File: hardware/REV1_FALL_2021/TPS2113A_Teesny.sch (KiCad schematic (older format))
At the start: 6 parts, among them U201 TPS2113ADRBR

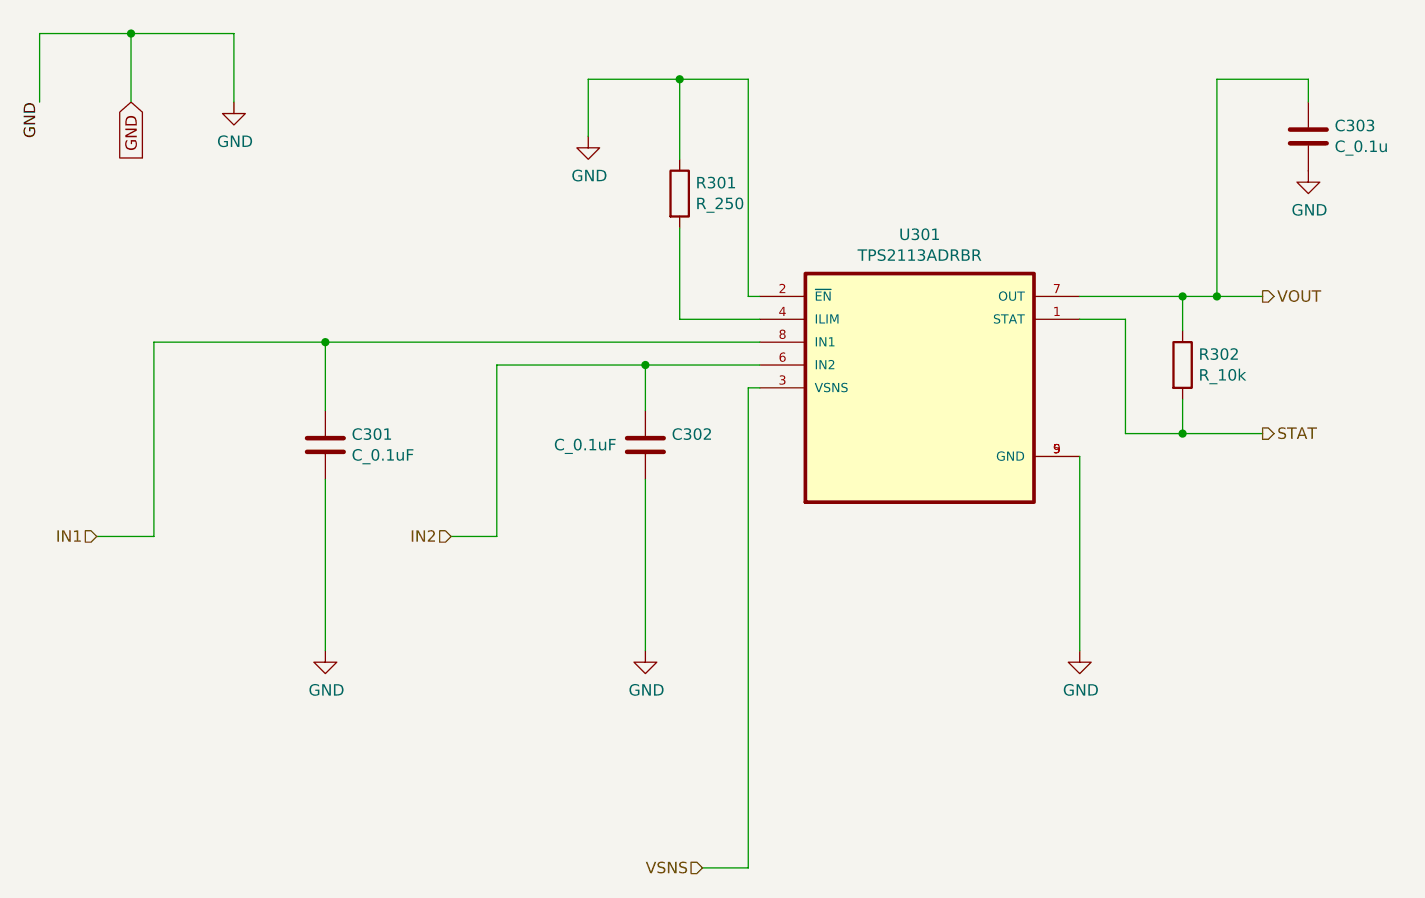
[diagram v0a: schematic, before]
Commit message: Change footprint of TPS2113A to the TSSOP package
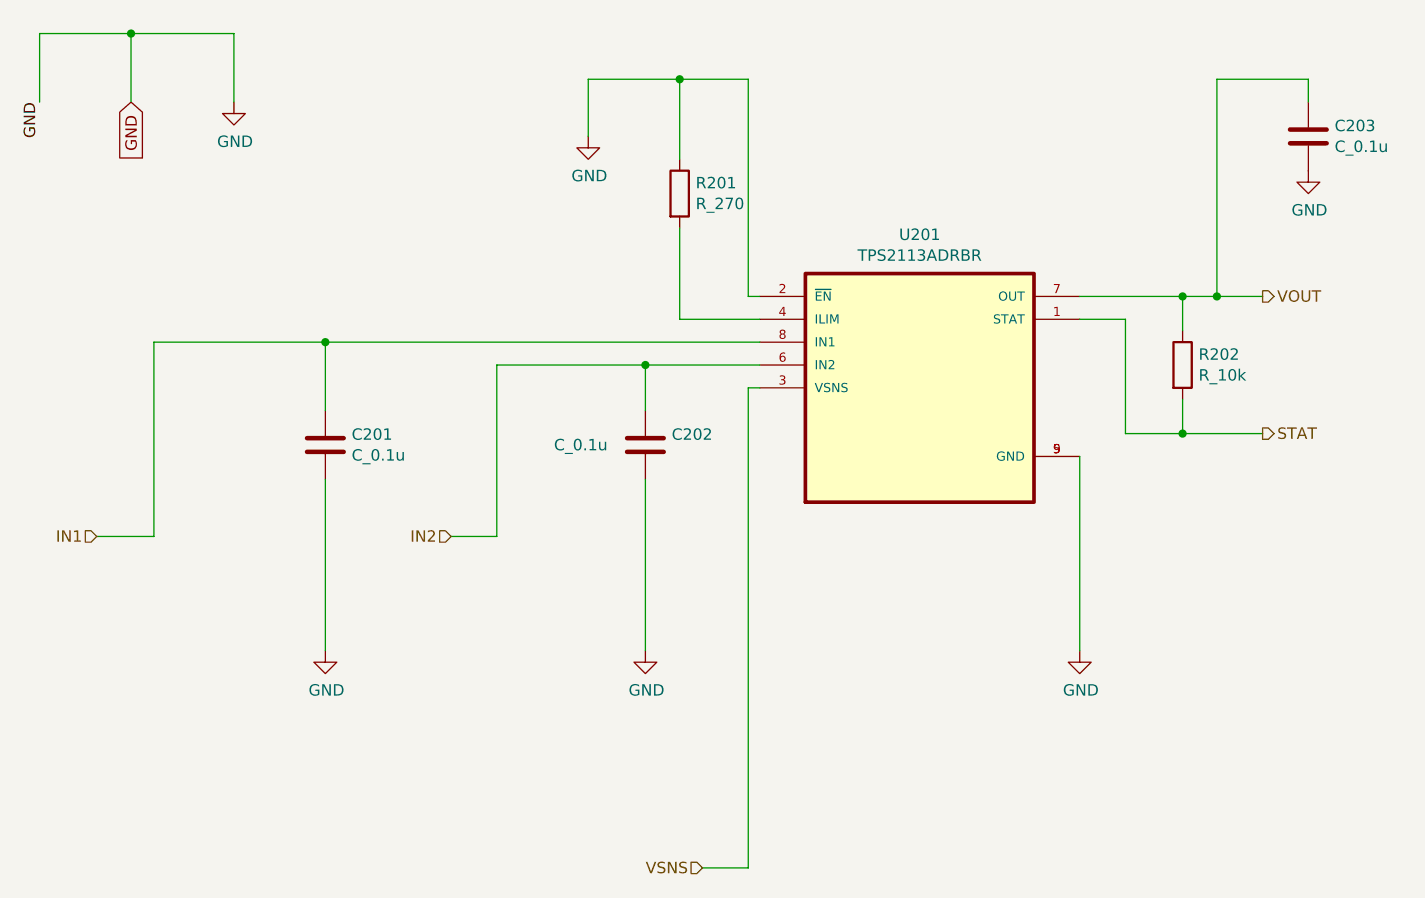
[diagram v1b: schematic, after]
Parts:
- C301, C302: value C_0.1uF -> C_0.1u
- R301: value R_250 -> R_270
- U201: footprint footprints:TPS2113ADRBR -> Package_SO:TSSOP-8_4.4x3mm_P0.65mm
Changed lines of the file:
@@
 AR Path="/61A02CEE/61AB462E" Ref="U201"  Part="1"
 AR Path="/619AC3BC/61AB462E" Ref="U301"  Part="1"
-F 0 "U301" H 6600 3720 50  0000 C CNN
+F 0 "U201" H 6600 3720 50  0000 C CNN
 F 1 "TPS2113ADRBR" H 6600 3629 50  0000 C CNN
-F 2 "footprints:TPS2113ADRBR" H 6600 3050 50  0001 L BNN
+F 2 "Package_SO:TSSOP-8_4.4x3mm_P0.65mm" H 6600 3050 50  0001 L BNN
 F 3 "https://www.ti.com/lit/ds/symlink/tps2113a.pdf" H 6600 3050 50  0001 L BNN
 	1    6600 3050
@@
 AR Path="/619AC3BC/61AB4644" Ref="C301"  Part="1"
 AR Path="/61A02CEE/61AB4644" Ref="C201"  Part="1"
-F 0 "C301" H 4115 3346 50  0000 L CNN
-F 1 "C_0.1uF" H 4115 3255 50  0000 L CNN
+F 0 "C201" H 4115 3346 50  0000 L CNN
+F 1 "C_0.1u" H 4115 3255 50  0000 L CNN
 F 2 "Capacitor_SMD:C_0805_2012Metric_Pad1.18x1.45mm_HandSolder" H 4038 3150 50  0001 C CNN
 F 3 "~" H 4000 3300 50  0001 C CNN
@@
 AR Path="/619AC3BC/61AB464C" Ref="C302"  Part="1"
 AR Path="/61A02CEE/61AB464C" Ref="C202"  Part="1"
-F 0 "C302" H 5515 3346 50  0000 L CNN
-F 1 "C_0.1uF" H 5000 3300 50  0000 L CNN
+F 0 "C202" H 5515 3346 50  0000 L CNN
+F 1 "C_0.1u" H 5000 3300 50  0000 L CNN
 F 2 "Capacitor_SMD:C_0805_2012Metric_Pad1.18x1.45mm_HandSolder" H 5438 3150 50  0001 C CNN
 F 3 "~" H 5400 3300 50  0001 C CNN
@@
 AR Path="/619AC3BC/61AB465E" Ref="R301"  Part="1"
 AR Path="/61A02CEE/61AB465E" Ref="R201"  Part="1"
-F 0 "R301" H 5620 2246 50  0000 L CNN
-F 1 "R_250" H 5620 2155 50  0000 L CNN
+F 0 "R201" H 5620 2246 50  0000 L CNN
+F 1 "R_270" H 5620 2155 50  0000 L CNN
 F 2 "Resistor_SMD:R_0805_2012Metric_Pad1.20x1.40mm_HandSolder" V 5480 2200 50  0001 C CNN
 F 3 "~" H 5550 2200 50  0001 C CNN
@@
 AR Path="/619AC3BC/61AB4669" Ref="#PWR0113"  Part="1"
 AR Path="/61A02CEE/61AB4669" Ref="#PWR0121"  Part="1"
-F 0 "#PWR0113" H 5150 1700 50  0001 C CNN
+F 0 "#PWR0121" H 5150 1700 50  0001 C CNN
 F 1 "GND" H 5155 1777 50  0000 C CNN
 F 2 "" H 5150 1950 50  0001 C CNN
@@
 AR Path="/619AC3BC/61AB4675" Ref="#PWR0115"  Part="1"
 AR Path="/61A02CEE/61AB4675" Ref="#PWR0123"  Part="1"
-F 0 "#PWR0115" H 4000 3950 50  0001 C CNN
+F 0 "#PWR0123" H 4000 3950 50  0001 C CNN
 F 1 "GND" H 4005 4027 50  0000 C CNN
 F 2 "" H 4000 4200 50  0001 C CNN
@@
 AR Path="/619AC3BC/61AB4681" Ref="#PWR0117"  Part="1"
 AR Path="/61A02CEE/61AB4681" Ref="#PWR0125"  Part="1"
-F 0 "#PWR0117" H 5400 3950 50  0001 C CNN
+F 0 "#PWR0125" H 5400 3950 50  0001 C CNN
 F 1 "GND" H 5405 4027 50  0000 C CNN
 F 2 "" H 5400 4200 50  0001 C CNN
@@
 AR Path="/619AC3BC/61AB4687" Ref="#PWR0118"  Part="1"
 AR Path="/61A02CEE/61AB4687" Ref="#PWR0126"  Part="1"
-F 0 "#PWR0118" H 7300 3950 50  0001 C CNN
+F 0 "#PWR0126" H 7300 3950 50  0001 C CNN
 F 1 "GND" H 7305 4027 50  0000 C CNN
 F 2 "" H 7300 4200 50  0001 C CNN
@@
 AR Path="/619AC3BC/61AB46B4" Ref="R302"  Part="1"
 AR Path="/61A02CEE/61AB46B4" Ref="R202"  Part="1"
-F 0 "R302" H 7820 2996 50  0000 L CNN
+F 0 "R202" H 7820 2996 50  0000 L CNN
 F 1 "R_10k" H 7820 2905 50  0000 L CNN
 F 2 "Resistor_SMD:R_0805_2012Metric_Pad1.20x1.40mm_HandSolder" V 7680 2950 50  0001 C CNN
@@
 AR Path="/619AC3BC/61AB46C3" Ref="C303"  Part="1"
 AR Path="/61A02CEE/61AB46C3" Ref="C203"  Part="1"
-F 0 "C303" H 8415 1996 50  0000 L CNN
+F 0 "C203" H 8415 1996 50  0000 L CNN
 F 1 "C_0.1u" H 8415 1905 50  0000 L CNN
 F 2 "Capacitor_SMD:C_0805_2012Metric_Pad1.18x1.45mm_HandSolder" H 8338 1800 50  0001 C CNN
@@
 AR Path="/619AC3BC/61AB46CF" Ref="#PWR0119"  Part="1"
 AR Path="/61A02CEE/61AB46CF" Ref="#PWR0127"  Part="1"
-F 0 "#PWR0119" H 8300 1850 50  0001 C CNN
+F 0 "#PWR0127" H 8300 1850 50  0001 C CNN
 F 1 "GND" H 8305 1927 50  0000 C CNN
 F 2 "" H 8300 2100 50  0001 C CNN
@@
 AR Path="/619AC3BC/61ABB0D4" Ref="#PWR0120"  Part="1"
 AR Path="/61A02CEE/61ABB0D4" Ref="#PWR0128"  Part="1"
-F 0 "#PWR0120" H 3600 1550 50  0001 C CNN
+F 0 "#PWR0128" H 3600 1550 50  0001 C CNN
 F 1 "GND" H 3605 1627 50  0000 C CNN
 F 2 "" H 3600 1800 50  0001 C CNN

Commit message: add series resistor to improve accuracy of ILIM resistor
It used to be a 400 ohm resistor, but those are not in stock in JLC's assembly parts. Now it is two 200 ohm resistors in series. It is important to get the values precise, because the maximum rating of the (inferior, but the only one in stock) TPS2113A is 1.25A, which is also the minimum all-fire current on the E-matches. So we need exactly 1.25A, not above, and not below.
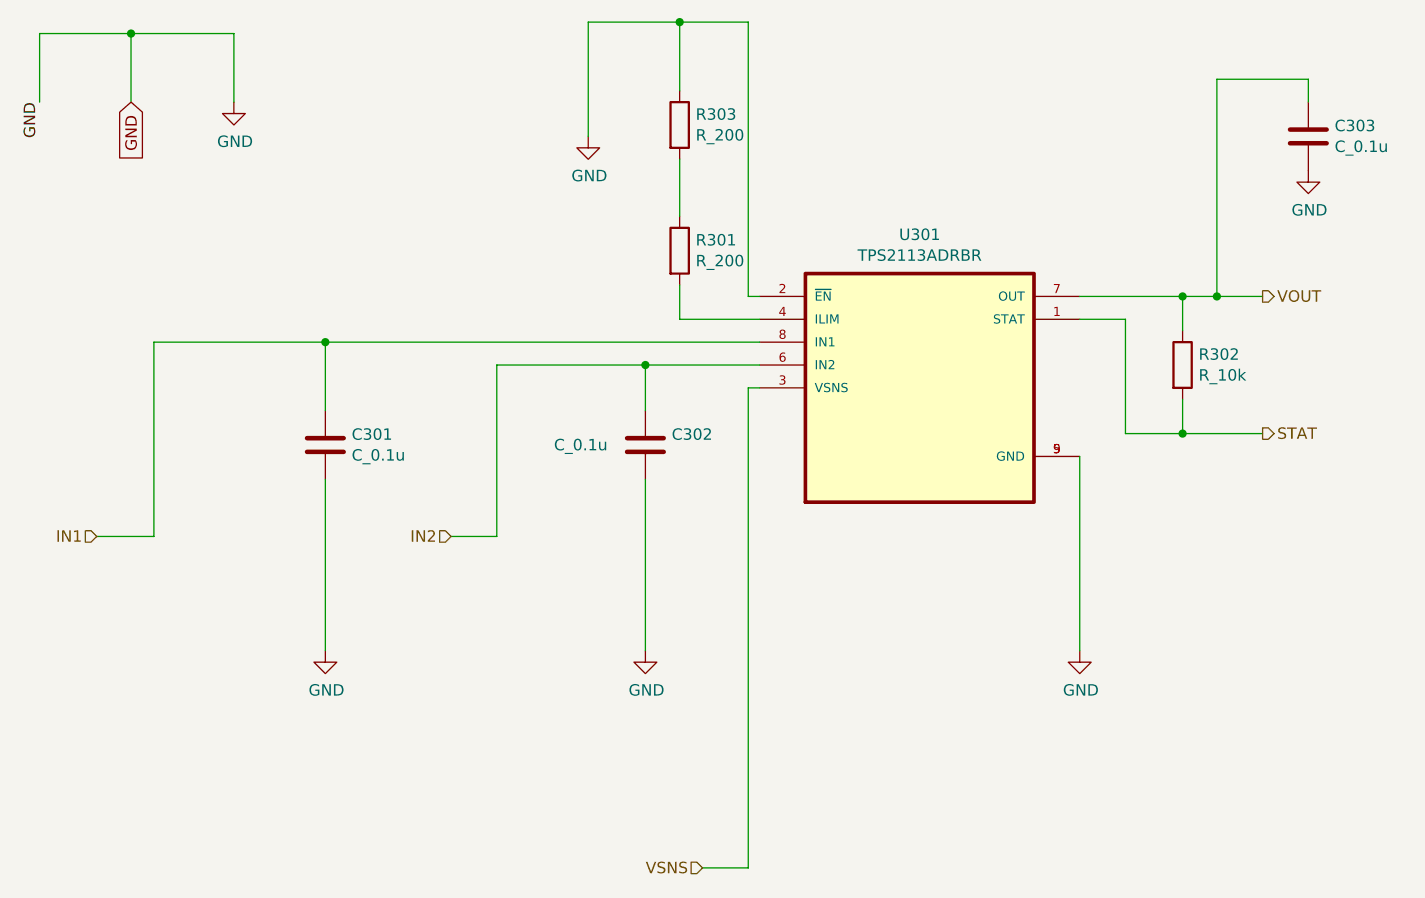
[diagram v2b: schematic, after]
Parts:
- added R303: R_200, Resistor_SMD:R_0805_2012Metric_Pad1.20x1.40mm_HandSolder, symbol Device:R
- R301: value R_270 -> R_200
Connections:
- net GND: now also R303.1; no longer R301.1
- new net: R301.1, R303.2
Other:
- moved on the sheet: R301
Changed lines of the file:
@@
 AR Path="/61A02CEE/61AB462E" Ref="U201"  Part="1"
 AR Path="/619AC3BC/61AB462E" Ref="U301"  Part="1"
-F 0 "U201" H 6600 3720 50  0000 C CNN
+F 0 "U301" H 6600 3720 50  0000 C CNN
 F 1 "TPS2113ADRBR" H 6600 3629 50  0000 C CNN
 F 2 "Package_SO:TSSOP-8_4.4x3mm_P0.65mm" H 6600 3050 50  0001 L BNN
@@
 AR Path="/619AC3BC/61AB4644" Ref="C301"  Part="1"
 AR Path="/61A02CEE/61AB4644" Ref="C201"  Part="1"
-F 0 "C201" H 4115 3346 50  0000 L CNN
+F 0 "C301" H 4115 3346 50  0000 L CNN
 F 1 "C_0.1u" H 4115 3255 50  0000 L CNN
 F 2 "Capacitor_SMD:C_0805_2012Metric_Pad1.18x1.45mm_HandSolder" H 4038 3150 50  0001 C CNN
@@
 AR Path="/619AC3BC/61AB464C" Ref="C302"  Part="1"
 AR Path="/61A02CEE/61AB464C" Ref="C202"  Part="1"
-F 0 "C202" H 5515 3346 50  0000 L CNN
+F 0 "C302" H 5515 3346 50  0000 L CNN
 F 1 "C_0.1u" H 5000 3300 50  0000 L CNN
 F 2 "Capacitor_SMD:C_0805_2012Metric_Pad1.18x1.45mm_HandSolder" H 5438 3150 50  0001 C CNN
@@
 	5900 2650 5850 2650
 Wire Wire Line
-	5850 2650 5850 1700
-Wire Wire Line
 	5900 2750 5550 2750
 Wire Wire Line
-	5550 2750 5550 2350
+	5550 2750 5550 2600
 $Comp
 L Device:R R?
 U 1 1 61AB465E
-P 5550 2200
+P 5550 2450
 AR Path="/61AB465E" Ref="R?"  Part="1"
 AR Path="/619AC3BC/61AB465E" Ref="R301"  Part="1"
 AR Path="/61A02CEE/61AB465E" Ref="R201"  Part="1"
-F 0 "R201" H 5620 2246 50  0000 L CNN
-F 1 "R_270" H 5620 2155 50  0000 L CNN
-F 2 "Resistor_SMD:R_0805_2012Metric_Pad1.20x1.40mm_HandSolder" V 5480 2200 50  0001 C CNN
-F 3 "~" H 5550 2200 50  0001 C CNN
-	1    5550 2200
-	1    0    0    -1
-$EndComp
-Wire Wire Line
-	5550 2050 5550 1700
-Wire Wire Line
-	5550 1700 5850 1700
-Wire Wire Line
-	5550 1700 5150 1700
-Wire Wire Line
-	5150 1700 5150 1950
-Connection ~ 5550 1700
+F 0 "R301" H 5620 2496 50  0000 L CNN
+F 1 "R_200" H 5620 2405 50  0000 L CNN
+F 2 "Resistor_SMD:R_0805_2012Metric_Pad1.20x1.40mm_HandSolder" V 5480 2450 50  0001 C CNN
+F 3 "~" H 5550 2450 50  0001 C CNN
+	1    5550 2450
+	1    0    0    -1
+$EndComp
+Wire Wire Line
+	5550 2300 5550 2050
 $Comp
 L power:GND #PWR?
@@
 AR Path="/619AC3BC/61AB4669" Ref="#PWR0113"  Part="1"
 AR Path="/61A02CEE/61AB4669" Ref="#PWR0121"  Part="1"
-F 0 "#PWR0121" H 5150 1700 50  0001 C CNN
+F 0 "#PWR0113" H 5150 1700 50  0001 C CNN
 F 1 "GND" H 5155 1777 50  0000 C CNN
 F 2 "" H 5150 1950 50  0001 C CNN
@@
 AR Path="/619AC3BC/61AB4675" Ref="#PWR0115"  Part="1"
 AR Path="/61A02CEE/61AB4675" Ref="#PWR0123"  Part="1"
-F 0 "#PWR0123" H 4000 3950 50  0001 C CNN
+F 0 "#PWR0115" H 4000 3950 50  0001 C CNN
 F 1 "GND" H 4005 4027 50  0000 C CNN
 F 2 "" H 4000 4200 50  0001 C CNN
@@
 AR Path="/619AC3BC/61AB4681" Ref="#PWR0117"  Part="1"
 AR Path="/61A02CEE/61AB4681" Ref="#PWR0125"  Part="1"
-F 0 "#PWR0125" H 5400 3950 50  0001 C CNN
+F 0 "#PWR0117" H 5400 3950 50  0001 C CNN
 F 1 "GND" H 5405 4027 50  0000 C CNN
 F 2 "" H 5400 4200 50  0001 C CNN
@@
 AR Path="/619AC3BC/61AB4687" Ref="#PWR0118"  Part="1"
 AR Path="/61A02CEE/61AB4687" Ref="#PWR0126"  Part="1"
-F 0 "#PWR0126" H 7300 3950 50  0001 C CNN
+F 0 "#PWR0118" H 7300 3950 50  0001 C CNN
 F 1 "GND" H 7305 4027 50  0000 C CNN
 F 2 "" H 7300 4200 50  0001 C CNN
@@
 AR Path="/619AC3BC/61AB46B4" Ref="R302"  Part="1"
 AR Path="/61A02CEE/61AB46B4" Ref="R202"  Part="1"
-F 0 "R202" H 7820 2996 50  0000 L CNN
+F 0 "R302" H 7820 2996 50  0000 L CNN
 F 1 "R_10k" H 7820 2905 50  0000 L CNN
 F 2 "Resistor_SMD:R_0805_2012Metric_Pad1.20x1.40mm_HandSolder" V 7680 2950 50  0001 C CNN
@@
 AR Path="/619AC3BC/61AB46C3" Ref="C303"  Part="1"
 AR Path="/61A02CEE/61AB46C3" Ref="C203"  Part="1"
-F 0 "C203" H 8415 1996 50  0000 L CNN
+F 0 "C303" H 8415 1996 50  0000 L CNN
 F 1 "C_0.1u" H 8415 1905 50  0000 L CNN
 F 2 "Capacitor_SMD:C_0805_2012Metric_Pad1.18x1.45mm_HandSolder" H 8338 1800 50  0001 C CNN
@@
 AR Path="/619AC3BC/61AB46CF" Ref="#PWR0119"  Part="1"
 AR Path="/61A02CEE/61AB46CF" Ref="#PWR0127"  Part="1"
-F 0 "#PWR0127" H 8300 1850 50  0001 C CNN
+F 0 "#PWR0119" H 8300 1850 50  0001 C CNN
 F 1 "GND" H 8305 1927 50  0000 C CNN
 F 2 "" H 8300 2100 50  0001 C CNN
@@
 AR Path="/619AC3BC/61ABB0D4" Ref="#PWR0120"  Part="1"
 AR Path="/61A02CEE/61ABB0D4" Ref="#PWR0128"  Part="1"
-F 0 "#PWR0128" H 3600 1550 50  0001 C CNN
+F 0 "#PWR0120" H 3600 1550 50  0001 C CNN
 F 1 "GND" H 3605 1627 50  0000 C CNN
 F 2 "" H 3600 1800 50  0001 C CNN
@@
 Wire Wire Line
 	3150 1500 3600 1500
+$Comp
+L Device:R R?
+U 1 1 619F982E
+P 5550 1900
+AR Path="/619F982E" Ref="R?"  Part="1"
+AR Path="/619AC3BC/619F982E" Ref="R303"  Part="1"
+AR Path="/61A02CEE/619F982E" Ref="R203"  Part="1"
+F 0 "R303" H 5620 1946 50  0000 L CNN
+F 1 "R_200" H 5620 1855 50  0000 L CNN
+F 2 "Resistor_SMD:R_0805_2012Metric_Pad1.20x1.40mm_HandSolder" V 5480 1900 50  0001 C CNN
+F 3 "~" H 5550 1900 50  0001 C CNN
+	1    5550 1900
+	1    0    0    -1
+$EndComp
+Wire Wire Line
+	5150 1450 5550 1450
+Wire Wire Line
+	5850 1450 5850 2650
+Wire Wire Line
+	5150 1450 5150 1950
+Wire Wire Line
+	5550 1450 5550 1750
+Connection ~ 5550 1450
+Wire Wire Line
+	5550 1450 5850 1450
 $EndSCHEMATC
